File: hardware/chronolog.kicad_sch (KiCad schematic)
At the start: 0 parts

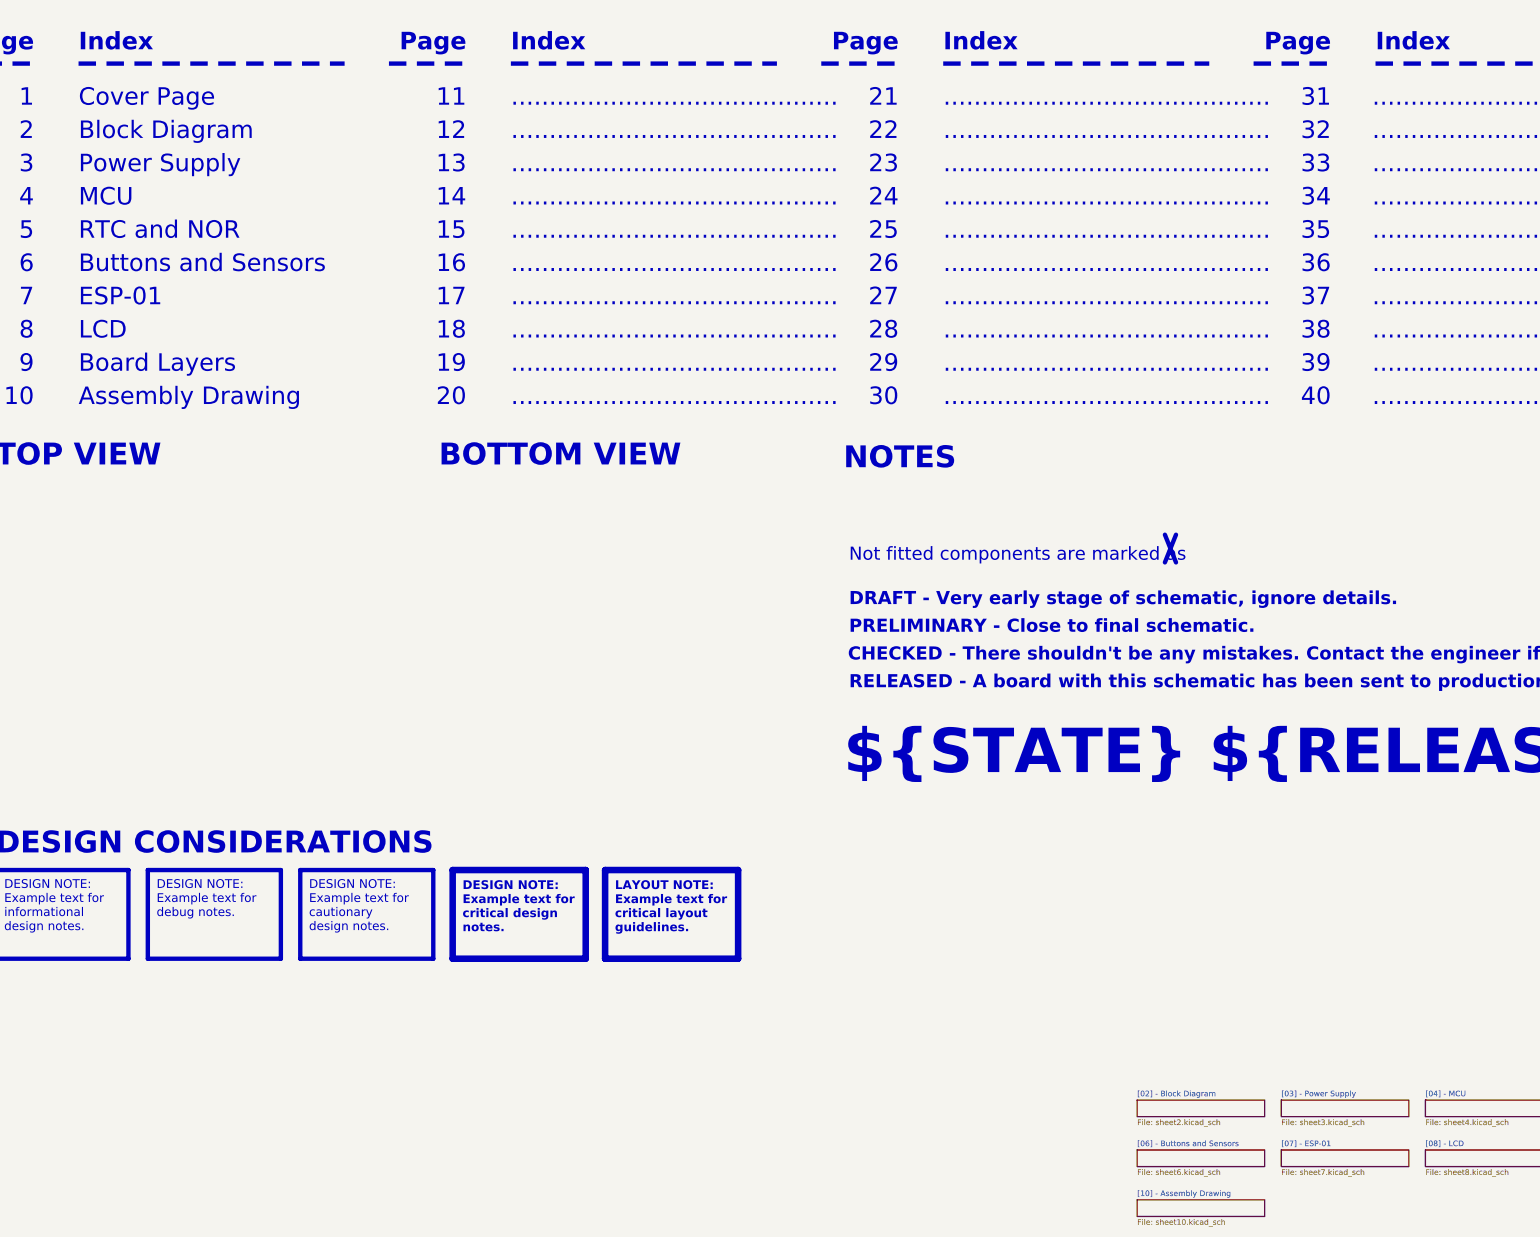
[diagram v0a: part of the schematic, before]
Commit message: hardware(feat): add assembly drawing
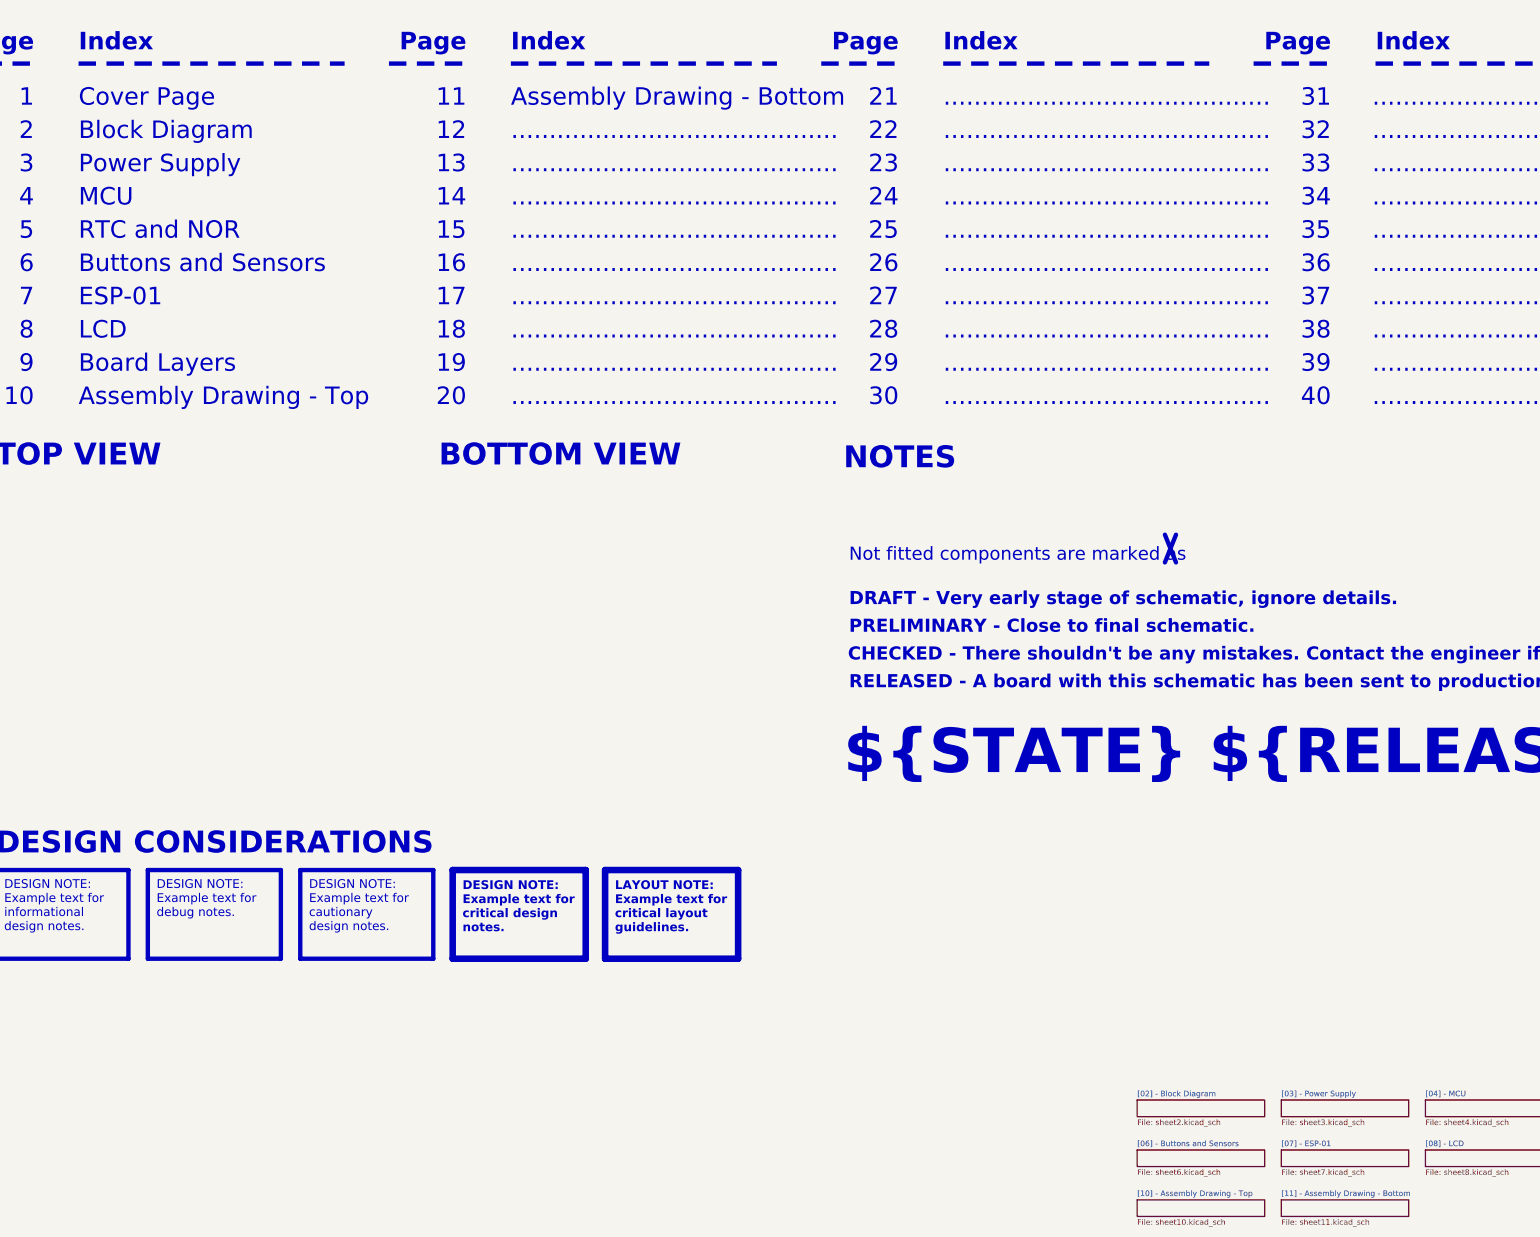
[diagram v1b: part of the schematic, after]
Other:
- sheet [10] - Assembly Drawing renamed [10] - Assembly Drawing - Top
- added sheet [11] - Assembly Drawing - Bottom (sheet11.kicad_sch)
- note added: "Assembly Drawing - Bottom"
- note added: "Assembly Drawing - Top"
- note removed: "Assembly Drawing"
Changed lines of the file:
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@@
 		)
 	)
-	(text "..........................................."
+	(text "Assembly Drawing - Bottom"
 		(exclude_from_sim no)
 		(at 143.51 80.01 0)
@@
 		)
 	)
-	(text "Assembly Drawing"
+	(text "Assembly Drawing - Top"
 		(exclude_from_sim no)
 		(at 44.45 148.59 0)
@@
 	)
 	(sheet
+		(at 320.04 330.2)
+		(size 29.21 3.81)
+		(exclude_from_sim no)
+		(in_bom yes)
+		(on_board yes)
+		(dnp no)
+		(fields_autoplaced yes)
+		(stroke
+			(width 0.1524)
+			(type solid)
+		)
+		(fill
+			(color 0 0 0 0.0000)
+		)
+		(property "Sheetname" "[11] - Assembly Drawing - Bottom"
+			(at 320.04 329.4884 0)
+			(effects
+				(font
+					(size 1.27 1.27)
+				)
+				(justify left bottom)
+			)
+		)
+		(property "Sheetfile" "sheet11.kicad_sch"
+			(at 320.04 334.5946 0)
+			(effects
+				(font
+					(size 1.27 1.27)
+				)
+				(justify left top)
+			)
+		)
+		(instances
+			(project "chronolog"
+				(path "/08767502-fa14-4976-aaca-9650785a2144"
+					(page "11")
+				)
+			)
+		)
+	)
+	(sheet
 		(at 320.04 318.77)
 		(size 29.21 3.81)
@@
 			(color 0 0 0 0.0000)
 		)
-		(property "Sheetname" "[10] - Assembly Drawing"
+		(property "Sheetname" "[10] - Assembly Drawing - Top"
 			(at 287.02 329.4884 0)
 			(effects
